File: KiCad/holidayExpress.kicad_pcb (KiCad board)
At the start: 2 copper layers, 50 x 50 mm, 21 parts, among them J1 motorPower, J2 motorPower, J3 batteryPower, J4 UARTprogrammer, U1 ESP32-PICO-MINI-02, U2 DRV8833, U3 MPM3610GQV-P

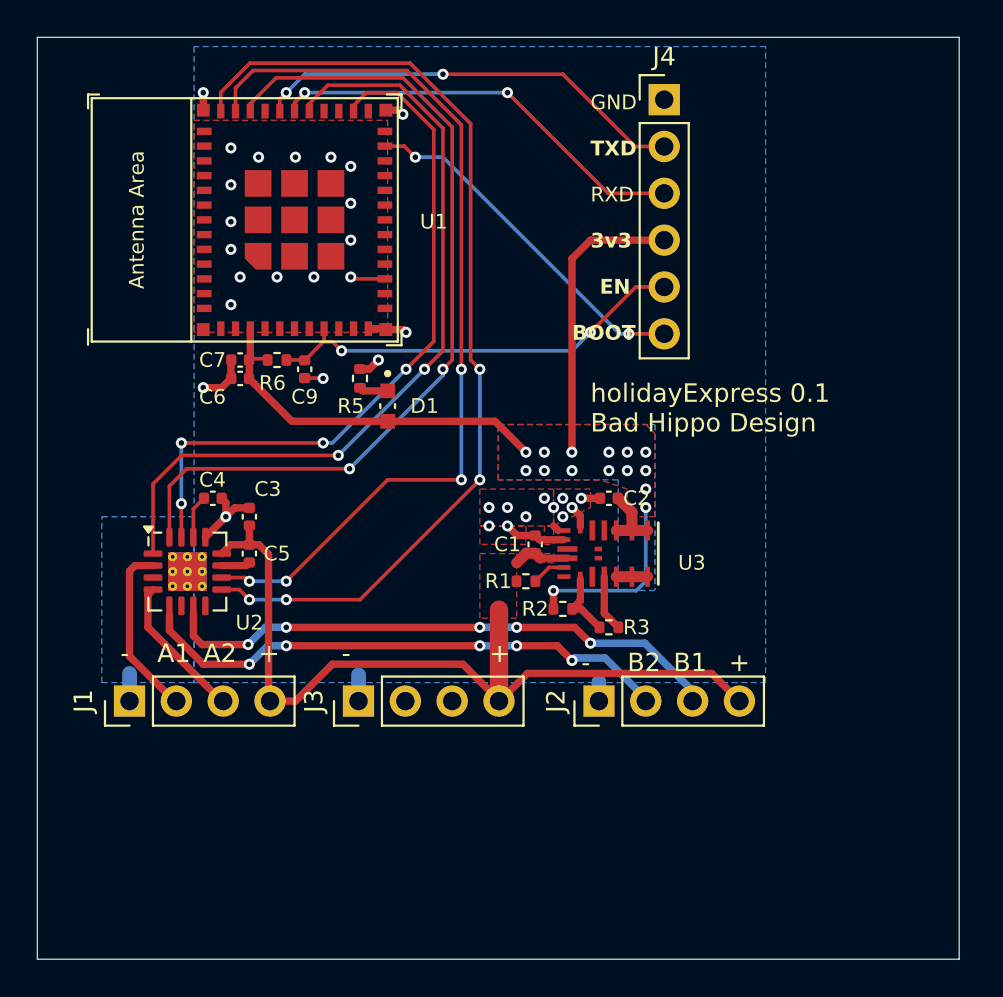
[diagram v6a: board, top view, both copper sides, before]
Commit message: improve copper fill areas and routing
Add copper fill zones with no thermal relief for SMD pads and use larger copper fills for 3.3V and 9V power planes.
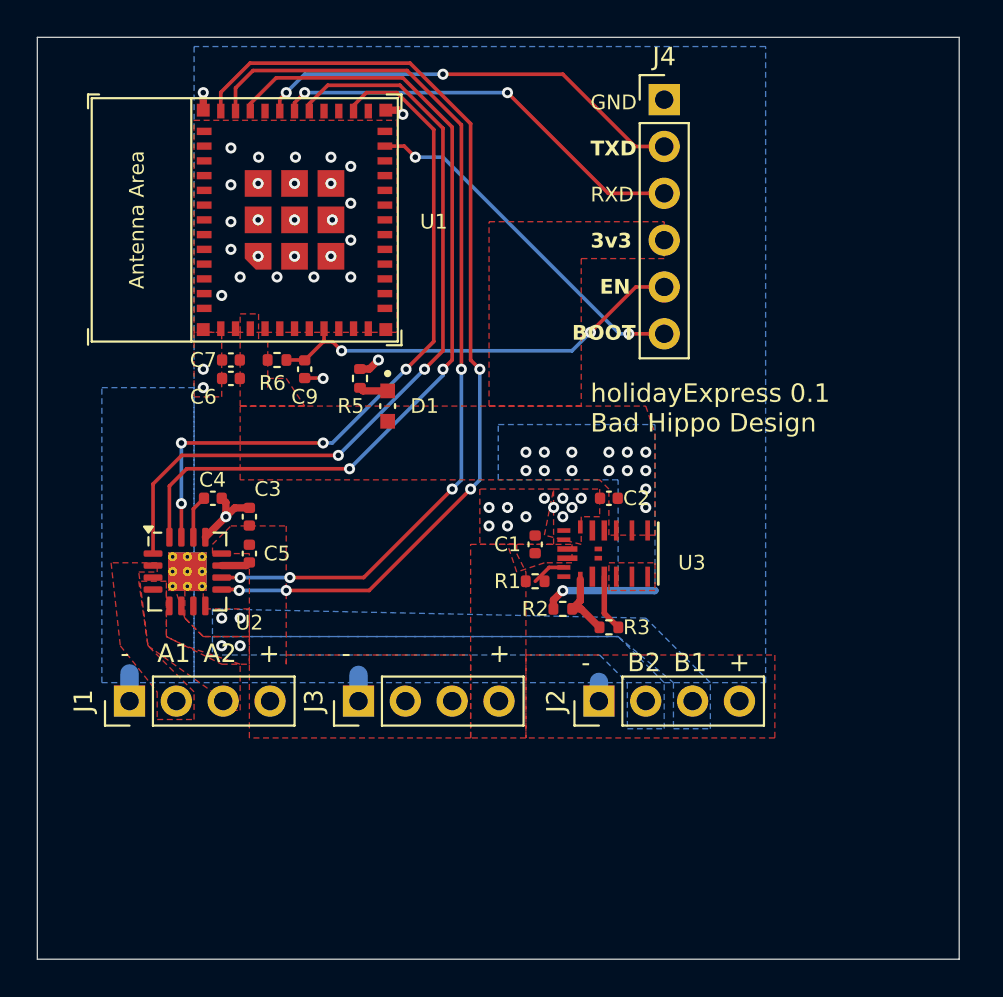
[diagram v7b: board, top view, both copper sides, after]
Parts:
- moved C6 0.50 mm to (168.5, 96.5)
- moved C7 0.50 mm to (168.5, 95.5)
- moved R1 0.50 mm to (185.0, 107.5)
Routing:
- net +9V: track 48.4 -> 0.02 mm
- net +3.3V: track 50.5 -> 6.56 mm
- net Net-(J2-Pin_3): track 31.3 -> 0.96 mm, vias 5 -> 2
- net Net-(J2-Pin_2): track 29.8 -> 0.13 mm, vias 5 -> 2
- net GND: track 26.5 -> 13.7 mm, vias 33 -> 42
- net Net-(J1-Pin_2): track 9.49 -> 0.03 mm
- net Net-(J1-Pin_3): track 7.82 -> 0.00 mm
- net Net-(U3-SW-Pad4): track 1.70 -> 0.00 mm
- added copper zone on F.Cu, net Net-(J1-Pin_2)
- added copper zone on F.Cu, net Net-(J1-Pin_3)
- added copper zone on B.Cu, net Net-(J2-Pin_2)
- added copper zone on F.Cu, net Net-(J2-Pin_2)
- added copper zone on B.Cu, net Net-(J2-Pin_3)
- added copper zone on F.Cu, net Net-(J2-Pin_3)
- added copper zone on F.Cu, net Net-(U3-SW-Pad4)

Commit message: fix DRV8833 to use correct symbol
Use QFN symbol so pin mapping matches footprint and part selection.
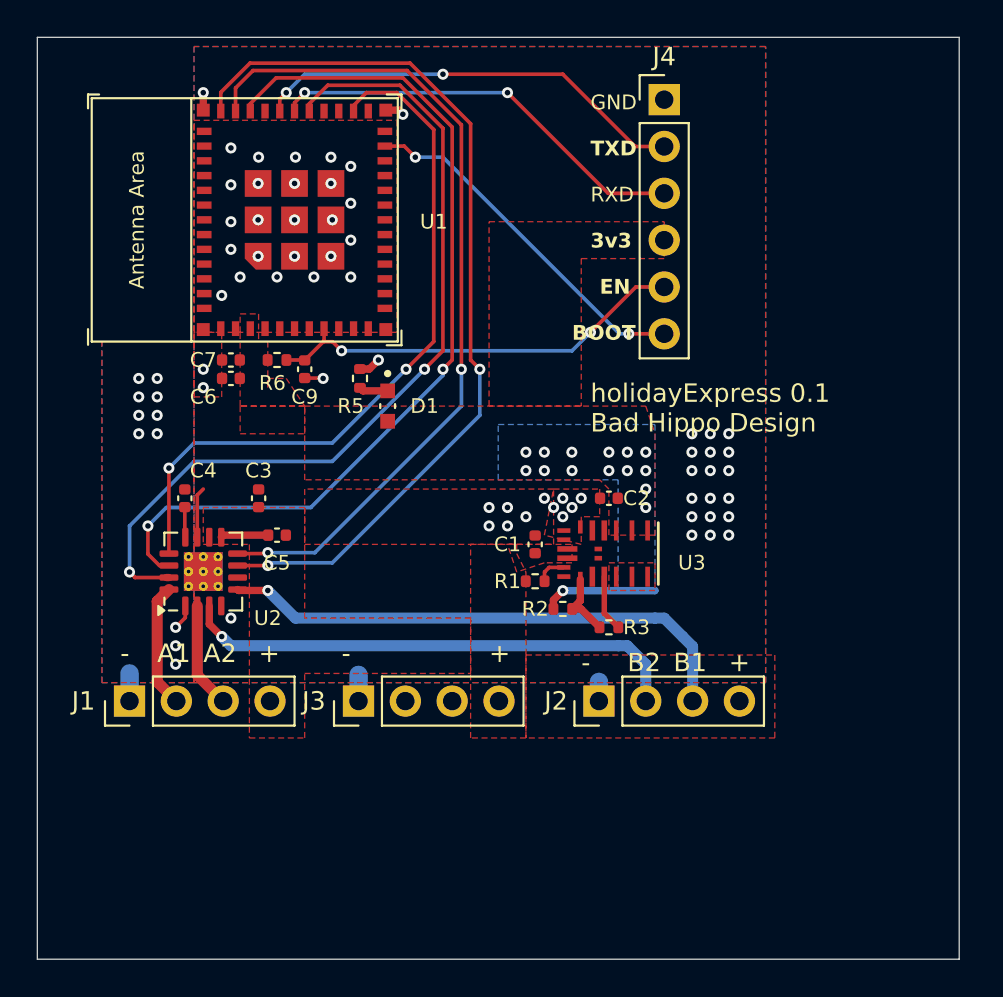
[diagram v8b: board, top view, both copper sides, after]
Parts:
- moved C5 1.80 mm to (171.0, 105.0), turned to 180 degrees
- moved C4 1.52 mm to (166.0, 103.0), turned to 90 degrees
- moved C3 1.12 mm to (170.0, 103.0)
- moved U2 0.86 mm to (167.0, 107.0), turned to 90 degrees
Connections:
- U2 pad 1: Net-(U1-GPIO5) -> GND
- U2 pad 10: Net-(U1-GPIO22) -> +9V
- U2 pad 11: Net-(U2-VCP) -> GND
- U2 pad 12: +9V -> Net-(U2-VINT)
- U2 pad 13: GND -> Net-(U1-GPIO20)
- U2 pad 14: Net-(U2-VINT) -> Net-(U1-GPIO19)
- U2 pad 15: Net-(U1-GPIO20) -> Net-(U1-GPIO5)
- U2 pad 16: Net-(U1-GPIO19) -> Net-(J1-Pin_2)
- U2 pad 17: (no net) -> GND
- U2 pad 2: Net-(J1-Pin_2) -> Net-(J1-Pin_3)
- U2 pad 3: unconnected-(U2-AISEN-Pad3) -> Net-(J2-Pin_2)
- U2 pad 4: Net-(J1-Pin_3) -> GND
- U2 pad 5: Net-(J2-Pin_2) -> Net-(J2-Pin_3)
- U2 pad 7: Net-(J2-Pin_3) -> Net-(U1-GPIO21)
- U2 pad 8: unconnected-(U2-~{FAULT}-Pad8) -> Net-(U1-GPIO22)
- U2 pad 9: Net-(U1-GPIO21) -> Net-(U2-VCP)
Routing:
- net Net-(J2-Pin_3): track 0.96 -> 29.5 mm, vias 2 -> 1
- net Net-(J2-Pin_2): track 0.13 -> 27.7 mm, vias 2 -> 1
- net Net-(J1-Pin_2): track 0.03 -> 6.77 mm
- net Net-(J1-Pin_3): track 0.00 -> 5.74 mm
- net Net-(U1-GPIO22): track 49.6 -> 45.8 mm, vias 4 -> 2
- net Net-(U1-GPIO21): track 52.6 -> 49.1 mm, vias 4 -> 2
- net Net-(U1-GPIO5): track 43.6 -> 46.9 mm
- net Net-(U1-GPIO19): track 46.8 -> 49.0 mm
- net Net-(U2-VCP): track 1.57 -> 2.59 mm
- net Net-(U1-GPIO20): track 38.3 -> 39.1 mm, vias 4 -> 2
- net Net-(U2-VINT): track 2.35 -> 1.64 mm
- net GND: vias 42 -> 71
- removed copper zone on F.Cu, net Net-(J1-Pin_2)
- removed copper zone on F.Cu, net Net-(J1-Pin_3)
- removed copper zone on B.Cu, net Net-(J2-Pin_2)
- removed copper zone on F.Cu, net Net-(J2-Pin_2)
- removed copper zone on B.Cu, net Net-(J2-Pin_3)
- removed copper zone on F.Cu, net Net-(J2-Pin_3)
